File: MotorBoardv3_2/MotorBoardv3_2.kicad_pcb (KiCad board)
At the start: 2 copper layers, 128.3 x 158.1 mm, 98 parts, among them J1 Bump0, J11 GP2Y0A41SK0F, J12 GP2Y0A41SK0F, J13 GP2Y0A41SK0F, J15 7.2, J16 LP5.0, J17 ELA, J18 ERA, J19 Voltage Display, J2 Bump1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

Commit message: Filled in ground plane where needed
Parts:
- moved H10 174.5 mm to (58.9, 58.3)
- moved J20 45.6 mm to (68.6, 159.4), turned to 180 degrees
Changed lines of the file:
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@@
 		)
 		(pad "4" thru_hole oval
-			(at 0 -6.260001 280)
+			(at 0 -6.260002 280)
 			(size 4.699 1.778)
 			(drill oval 4.191 1.016)
@@
 	(footprint "RSLK2:54-00127_TEN"
 		(layer "F.Cu")
-		(at 98.689999 193.739955)
+		(at 68.600001 159.430045 180)
 		(tags "54-00127 ")
 		(property "Reference" "J20"
-			(at 4.650001 0 0)
+			(at 4.650001 0 180)
 			(unlocked yes)
 			(layer "F.SilkS")
@@
 		)
 		(property "Value" "Barrel_Jack"
-			(at 4.650001 0 0)
+			(at 4.650001 0 180)
 			(unlocked yes)
 			(layer "F.Fab")
@@
 		)
 		(property "Footprint" "RSLK2:54-00127_TEN"
-			(at 0 0 0)
+			(at 0 0 360)
 			(layer "F.Fab")
 			(hide yes)
@@
 		)
 		(property "Datasheet" ""
-			(at 0 0 0)
+			(at 0 0 360)
 			(layer "F.Fab")
 			(hide yes)
@@
 		)
 		(property "Description" "DC Barrel Jack"
-			(at 0 0 0)
+			(at 0 0 360)
 			(layer "F.Fab")
 			(hide yes)
@@
 		(attr smd)
 		(fp_line
-			(start -0.526999 -10.426954)
-			(end -0.526999 -9.016105)
+			(start 9.827001 1.333246)
+			(end 9.827001 -5.583806)
 			(stroke
 				(width 0.1524)
@@
 		)
 		(fp_line
-			(start -0.526999 -5.583806)
-			(end -0.526999 -1.438684)
+			(start 9.827001 -9.016105)
+			(end 9.827001 -10.426954)
 			(stroke
 				(width 0.1524)
@@
 		)
 		(fp_line
-			(start 0.666425 1.333246)
-			(end 2.733526 1.333246)
+			(start 9.827001 -10.426954)
+			(end -0.526999 -10.426954)
 			(stroke
 				(width 0.1524)
@@
 		)
 		(fp_line
-			(start 4.066476 1.333246)
-			(end 7.933576 1.333246)
+			(start 9.266425 1.333246)
+			(end 9.827001 1.333246)
 			(stroke
 				(width 0.1524)
@@
 		)
 		(fp_line
-			(start 4.523001 -10.426954)
-			(end 4.523001 -10.172954)
+			(start 4.777001 -10.172954)
+			(end 4.777001 -10.426954)
 			(stroke
 				(width 0.1524)
@@
 		)
 		(fp_line
-			(start 4.523001 -10.172954)
-			(end 4.777001 -10.172954)
+			(start 4.777001 -10.426954)
+			(end 4.523001 -10.426954)
 			(stroke
 				(width 0.1524)
@@
 		)
 		(fp_line
-			(start 4.777001 -10.426954)
-			(end 4.523001 -10.426954)
+			(start 4.523001 -10.172954)
+			(end 4.777001 -10.172954)
 			(stroke
 				(width 0.1524)
@@
 		)
 		(fp_line
-			(start 4.777001 -10.172954)
-			(end 4.777001 -10.426954)
+			(start 4.523001 -10.426954)
+			(end 4.523001 -10.172954)
 			(stroke
 				(width 0.1524)
@@
 		)
 		(fp_line
-			(start 9.266425 1.333246)
-			(end 9.827001 1.333246)
+			(start 4.066476 1.333246)
+			(end 7.933576 1.333246)
 			(stroke
 				(width 0.1524)
@@
 		)
 		(fp_line
-			(start 9.827001 -10.426954)
-			(end -0.526999 -10.426954)
+			(start 0.666425 1.333246)
+			(end 2.733526 1.333246)
 			(stroke
 				(width 0.1524)
@@
 		)
 		(fp_line
-			(start 9.827001 -9.016105)
-			(end 9.827001 -10.426954)
+			(start -0.526999 -5.583806)
+			(end -0.526999 -1.438684)
 			(stroke
 				(width 0.1524)
@@
 		)
 		(fp_line
-			(start 9.827001 1.333246)
-			(end 9.827001 -5.583806)
+			(start -0.526999 -10.426954)
+			(end -0.526999 -9.016105)
 			(stroke
 				(width 0.1524)
@@
 		)
 		(fp_line
-			(start -0.653999 -10.553954)
-			(end -0.653999 1.460246)
+			(start 9.954001 1.460246)
+			(end 9.954001 -10.553954)
 			(stroke
 				(width 0.1524)
@@
 		)
 		(fp_line
-			(start -0.653999 1.460246)
-			(end 9.954001 1.460246)
+			(start 9.954001 -10.553954)
+			(end -0.653999 -10.553954)
 			(stroke
 				(width 0.1524)
@@
 		)
 		(fp_line
-			(start 9.954001 -10.553954)
-			(end -0.653999 -10.553954)
+			(start -0.653999 1.460246)
+			(end 9.954001 1.460246)
 			(stroke
 				(width 0.1524)
@@
 		)
 		(fp_line
-			(start 9.954001 1.460246)
-			(end 9.954001 -10.553954)
+			(start -0.653999 -10.553954)
+			(end -0.653999 1.460246)
 			(stroke
 				(width 0.1524)
@@
 		)
 		(fp_line
-			(start -0.399999 -10.299954)
-			(end -0.399999 1.206246)
+			(start 9.700001 1.206246)
+			(end 9.700001 -10.299954)
 			(stroke
 				(width 0.0254)
@@
 		)
 		(fp_line
-			(start -0.399999 1.206246)
-			(end 9.700001 1.206246)
+			(start 9.700001 -10.299954)
+			(end -0.399999 -10.299954)
 			(stroke
 				(width 0.0254)
@@
 		)
 		(fp_line
-			(start 9.700001 -10.299954)
-			(end -0.399999 -10.299954)
+			(start -0.399999 1.206246)
+			(end 9.700001 1.206246)
 			(stroke
 				(width 0.0254)
@@
 		)
 		(fp_line
-			(start 9.700001 1.206246)
-			(end 9.700001 -10.299954)
+			(start -0.399999 -10.299954)
+			(end -0.399999 1.206246)
 			(stroke
 				(width 0.0254)
@@
 		)
 		(fp_text user "*"
-			(at -2.54 0 0)
+			(at -2.54 0 180)
 			(unlocked yes)
 			(layer "F.SilkS")
@@
 		)
 		(fp_text user "*"
-			(at -2.54 0 0)
+			(at -2.54 0 360)
 			(layer "F.SilkS")
 			(effects
@@
 		)
 		(fp_text user "*"
-			(at -2.54 0 0)
+			(at -2.54 0 360)
 			(layer "F.Fab")
 			(effects
@@
 		)
 		(fp_text user "${REFERENCE}"
-			(at 4.650001 0 0)
+			(at 4.650001 0 180)
 			(unlocked yes)
 			(layer "F.Fab")
@@
 		)
 		(fp_text user "*"
-			(at -2.54 0 0)
+			(at -2.54 0 180)
 			(unlocked yes)
 			(layer "F.Fab")
@@
 		)
 		(pad "" np_thru_hole circle
-			(at 3.300001 -6.299955)
+			(at 3.300001 -6.299955 180)
 			(size 2.54 2.54)
 			(drill 2.54)
@@
 		)
 		(pad "1" smd oval
-			(at 0 0)
+			(at 0 0 180)
 			(size 1.3208 2.5146)
 			(layers "F.Cu" "F.Paste" "F.Mask")
@@
 		)
 		(pad "2" smd oval
-			(at 8.600001 0)
+			(at 8.600001 0 180)
 			(size 1.3208 2.5146)
 			(layers "F.Cu" "F.Paste" "F.Mask")
@@
 		)
 		(pad "3" smd oval
-			(at 3.400001 0)
+			(at 3.400001 0 180)
 			(size 1.3208 2.5146)
 			(layers "F.Cu" "F.Paste" "F.Mask")
 		)
 		(pad "4" smd oval
-			(at -0.299999 -7.299955)
+			(at -0.299999 -7.299955 180)
 			(size 1.3208 2.8194)
 			(layers "F.Cu" "F.Paste" "F.Mask")
 		)
 		(pad "5" smd oval
-			(at 9.600001 -7.299955)
+			(at 9.600001 -7.299955 180)
 			(size 1.3208 2.8194)
 			(layers "F.Cu" "F.Paste" "F.Mask")
@@
 	(footprint "RSLK2:MountingHole_4_40"
 		(layer "F.Cu")
-		(at 231.71 82.86)
+		(at 58.92 58.31)
 		(descr "Mounting Hole 0.125in")
 		(tags "mounting hole 0.125in 4_40")
@@
 		(tags "mounting hole 0.125in 4_40")
 		(property "Reference" "H21"
-			(at 0 -4 0)
+			(at 0.05 11.2 0)
 			(layer "F.SilkS")
 			(effects
@@
 		)
 		(pad "4" thru_hole oval
-			(at 0 6.260001 260)
+			(at 0 6.260002 260)
 			(size 4.699 1.778)
 			(drill oval 4.191 1.016)
@@
 	)
 	(zone
+		(net 1)
+		(net_name "GND")
+		(layer "B.Cu")
+		(hatch edge 0.5)
+		(connect_pads
+			(clearance 0.5)
+		)
+		(min_thickness 0.25)
+		(filled_areas_thickness no)
+		(fill yes
+			(thermal_gap 0.5)
+			(thermal_bridge_width 0.5)
+		)
+		(polygon
+			(pts
+				(xy 50.16 156.83) (xy 58.45 170.2) (xy 107.31 182.26) (xy 159.52 167.26) (xy 166.71 156.87) (xy 162.56 156.85)
+				(xy 162.53 148.6) (xy 152.4 148.58) (xy 152.34 156.84) (xy 50.24 156.86)
+			)
+		)
+	)
+	(zone

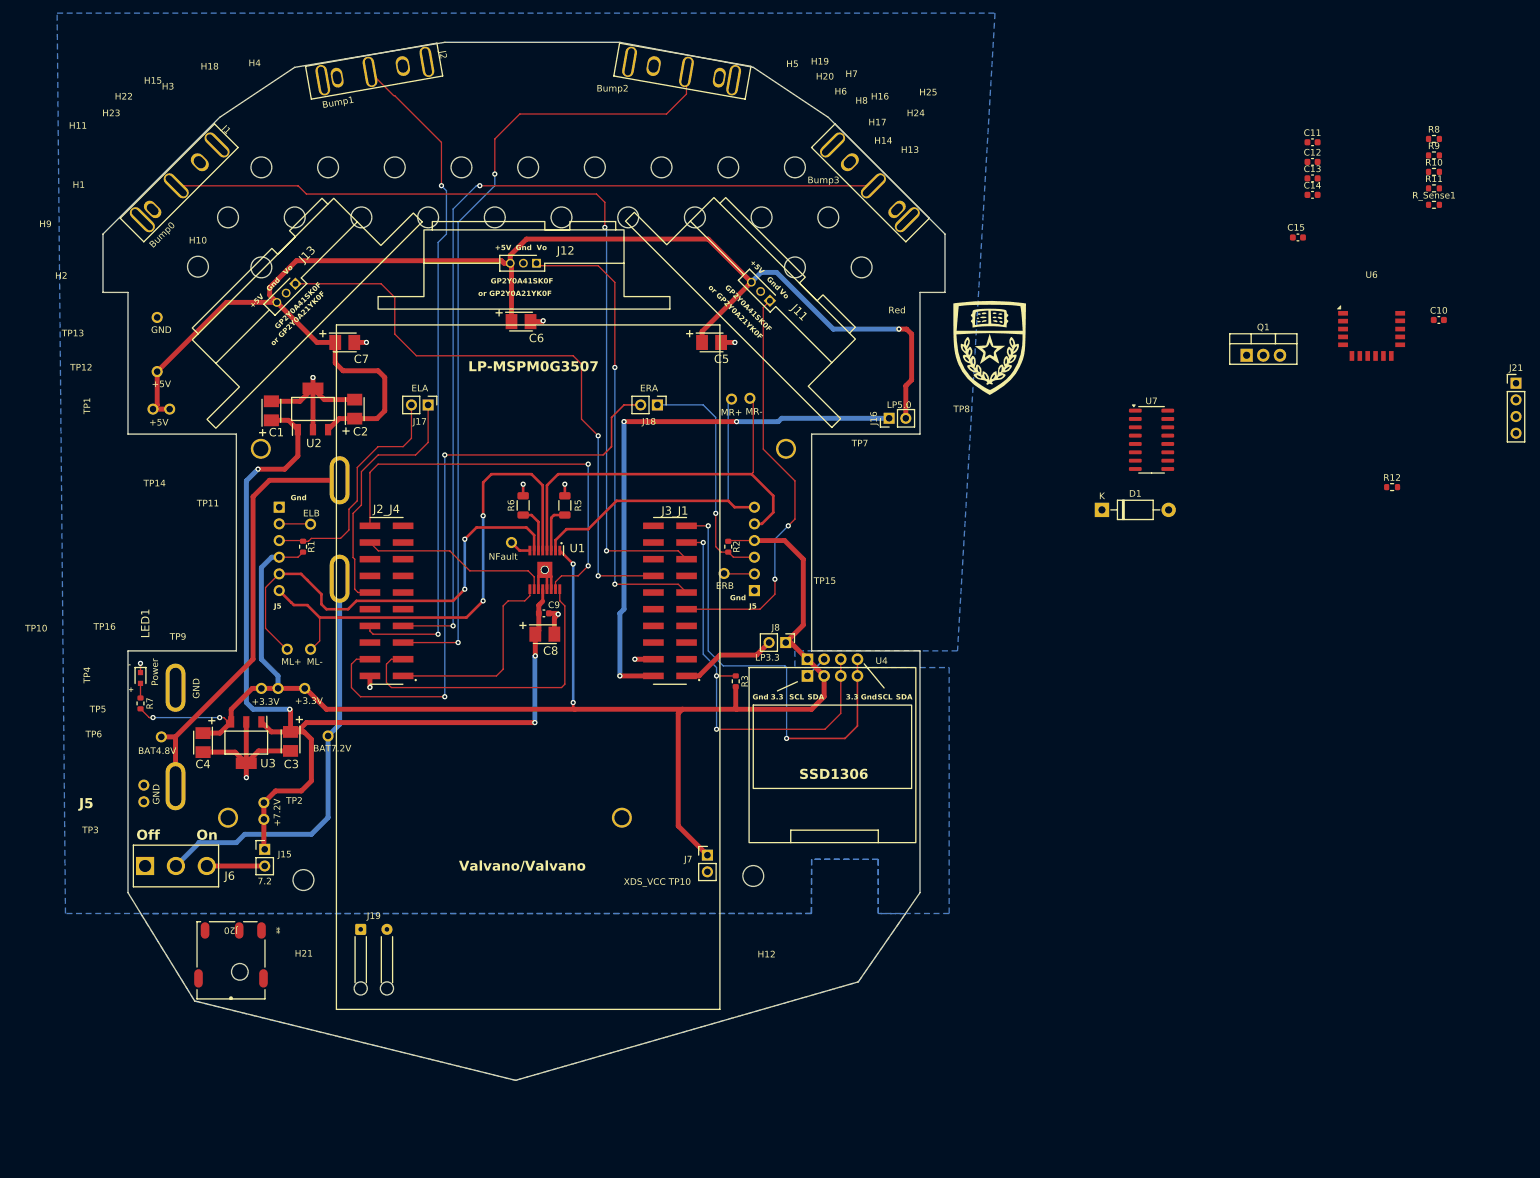
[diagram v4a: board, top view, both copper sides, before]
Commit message: Initial Charge Controller layout
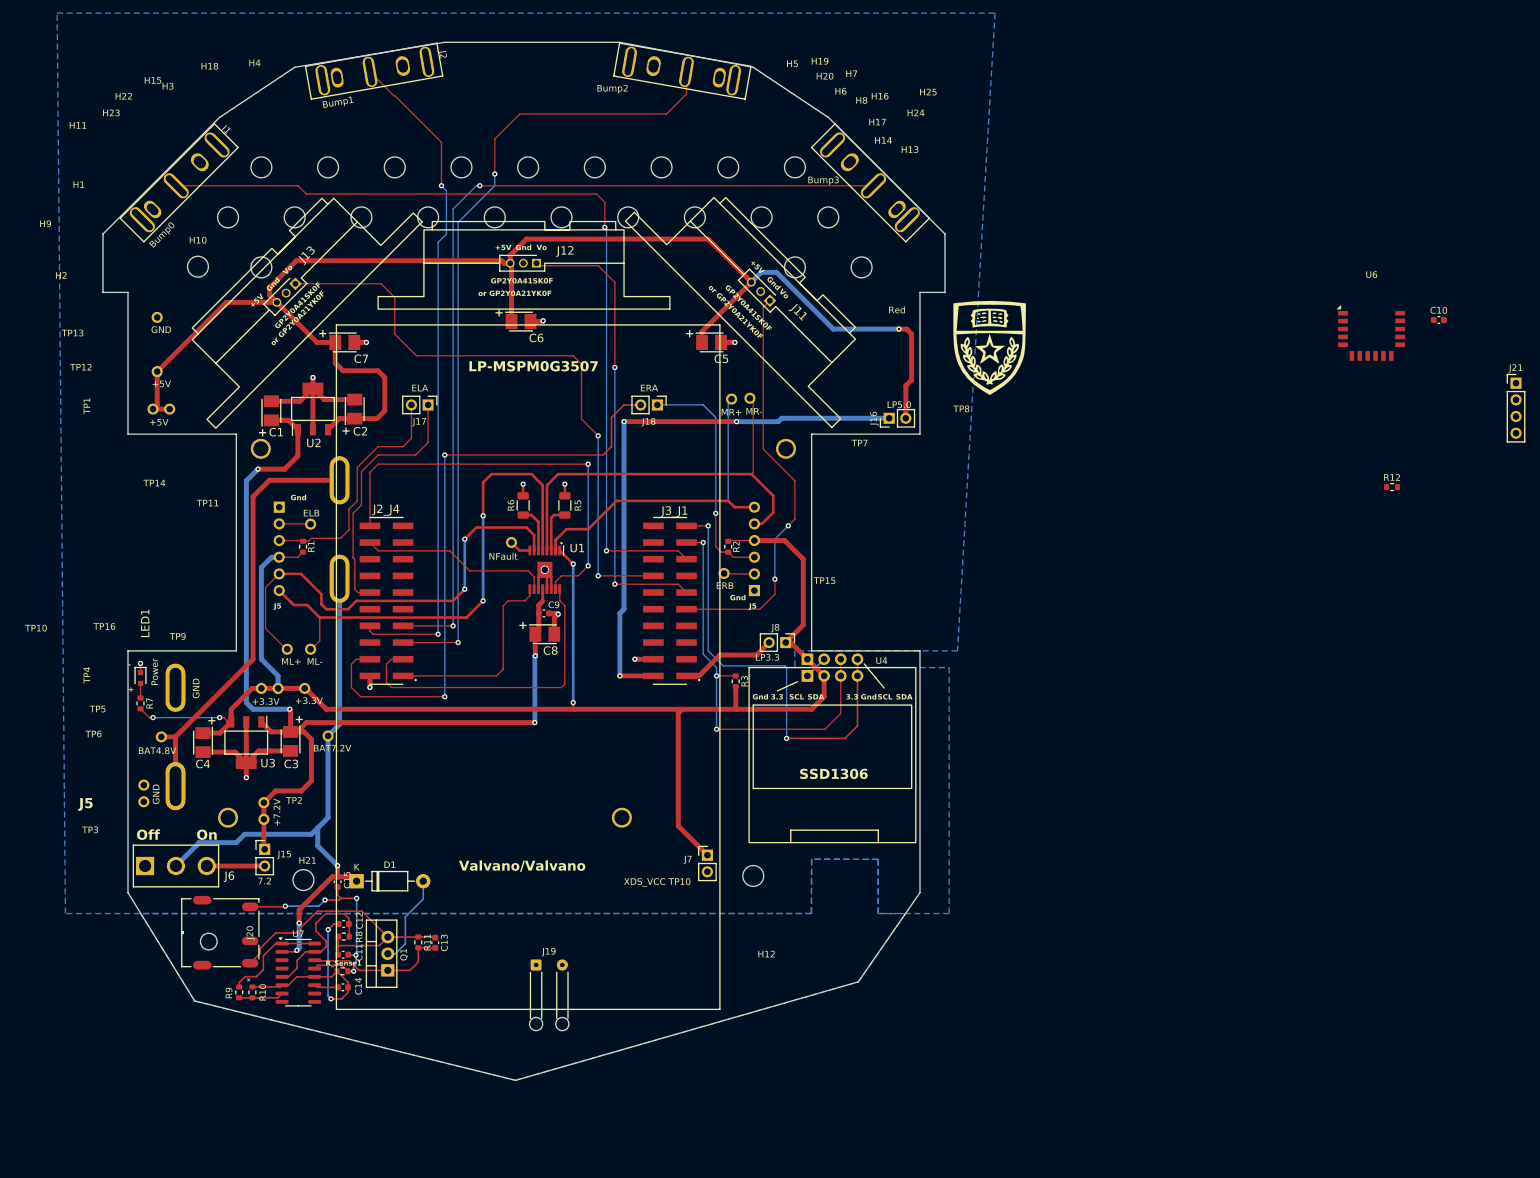
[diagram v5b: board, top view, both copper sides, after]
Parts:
- moved R9 222.2 mm to (65.2, 168.9), turned to -90 degrees
- moved R10 219.1 mm to (67.2, 168.9), turned to 90 degrees
- moved R8 205.8 mm to (81.1, 160.4)
- moved R_Sense1 203.2 mm to (80.9, 165.7)
- moved R11 192.7 mm to (92.5, 161.2), turned to -90 degrees
- moved C11 192.7 mm to (81.0, 163.1)
- moved C14 190.8 mm to (81.0, 168.1)
- moved C12 187.8 mm to (81.1, 158.4), turned to 180 degrees
- moved C13 177.3 mm to (95.1, 161.3), turned to -90 degrees
- moved C15 176.2 mm to (80.2, 152.0), turned to -90 degrees
- moved Q1 160.9 mm to (87.8, 165.5), turned to 90 degrees
- moved U7 153.2 mm to (74.2, 165.9)
- moved D1 126.9 mm to (83.1, 151.9)
- moved J19 27.3 mm to (110.4, 164.7)
- moved J20 5.28 mm to (66.9, 164.4), turned to 90 degrees
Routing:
- net Net-(Q1-E): track 0.00 -> 44.5 mm
- net Net-(U7-GND): track 0.00 -> 37.8 mm, vias 0 -> 5
- net GND: track 80.0 -> 113.5 mm, vias 12 -> 14
- net BAT7.2V: track 63.4 -> 91.9 mm, vias 0 -> 3
- net Net-(U7-THI): track 0.00 -> 22.6 mm
- net Net-(Q1-B): track 0.00 -> 21.7 mm
- net Net-(U7-REF): track 0.00 -> 15.9 mm
- net Net-(D1-A): track 0.00 -> 14.0 mm
- net Net-(U7-TEMP): track 0.00 -> 6.79 mm
- net Net-(U7-CC): track 0.00 -> 4.44 mm

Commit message: Label adjustements
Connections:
- net Net-(Q1-B) renamed /Charge Circuit/DRV
- net Net-(U7-REF) renamed /Charge Circuit/REF
- net Net-(U7-TEMP) renamed /Charge Circuit/TEMP
- net Net-(U7-THI) renamed /Charge Circuit/V+
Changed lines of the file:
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@@
 	(net 72 "Net-(Q1-E)")
 	(net 73 "Net-(U7-GND)")
-	(net 74 "Net-(U7-THI)")
-	(net 75 "Net-(Q1-B)")
+	(net 74 "/Charge Circuit/V+")
+	(net 75 "/Charge Circuit/DRV")
 	(net 76 "Net-(U7-CC)")
 	(net 77 "Net-(D1-A)")
-	(net 78 "Net-(U7-REF)")
-	(net 79 "Net-(U7-TEMP)")
+	(net 78 "/Charge Circuit/REF")
+	(net 79 "/Charge Circuit/TEMP")
 	(net 80 "unconnected-(U6-P1_7-Pad5)")
 	(net 81 "unconnected-(U6-RST-Pad10)")
@@
 			(layers "F.Cu" "F.Paste" "F.Mask")
 			(roundrect_rratio 0.25)
-			(net 74 "Net-(U7-THI)")
+			(net 74 "/Charge Circuit/V+")
 			(pintype "passive")
 		)
@@
 			(layers "F.Cu" "F.Paste" "F.Mask")
 			(roundrect_rratio 0.25)
-			(net 79 "Net-(U7-TEMP)")
+			(net 79 "/Charge Circuit/TEMP")
 			(pintype "passive")
 		)
@@
 			(layers "F.Cu" "F.Paste" "F.Mask")
 			(roundrect_rratio 0.25)
-			(net 75 "Net-(Q1-B)")
+			(net 75 "/Charge Circuit/DRV")
 			(pintype "passive")
 		)
@@
 			(layers "F.Cu" "F.Paste" "F.Mask")
 			(roundrect_rratio 0.25)
-			(net 74 "Net-(U7-THI)")
+			(net 74 "/Charge Circuit/V+")
 			(pintype "passive")
 		)
@@
 			(layers "*.Cu" "*.Mask")
 			(remove_unused_layers no)
-			(net 75 "Net-(Q1-B)")
+			(net 75 "/Charge Circuit/DRV")
 			(pinfunction "B")
 			(pintype "input")
@@
 			(layers "F.Cu" "F.Paste" "F.Mask")
 			(roundrect_rratio 0.25)
-			(net 78 "Net-(U7-REF)")
+			(net 78 "/Charge Circuit/REF")
 			(pinfunction "VLIMIT")
 			(pintype "input")
@@
 			(layers "F.Cu" "F.Paste" "F.Mask")
 			(roundrect_rratio 0.25)
-			(net 74 "Net-(U7-THI)")
+			(net 74 "/Charge Circuit/V+")
 			(pinfunction "THI")
 			(pintype "input")
@@
 			(layers "F.Cu" "F.Paste" "F.Mask")
 			(roundrect_rratio 0.25)
-			(net 79 "Net-(U7-TEMP)")
+			(net 79 "/Charge Circuit/TEMP")
 			(pinfunction "TEMP")
 			(pintype "input")
@@
 			(layers "F.Cu" "F.Paste" "F.Mask")
 			(roundrect_rratio 0.25)
-			(net 75 "Net-(Q1-B)")
+			(net 75 "/Charge Circuit/DRV")
 			(pinfunction "DRV")
 			(pintype "output")
@@
 			(layers "F.Cu" "F.Paste" "F.Mask")
 			(roundrect_rratio 0.25)
-			(net 74 "Net-(U7-THI)")
+			(net 74 "/Charge Circuit/V+")
 			(pinfunction "V+")
 			(pintype "power_in")
@@
 			(layers "F.Cu" "F.Paste" "F.Mask")
 			(roundrect_rratio 0.25)
-			(net 78 "Net-(U7-REF)")
+			(net 78 "/Charge Circuit/REF")
 			(pinfunction "REF")
 			(pintype "power_in")
@@
 			(layers "F.Cu" "F.Paste" "F.Mask")
 			(roundrect_rratio 0.25)
-			(net 75 "Net-(Q1-B)")
+			(net 75 "/Charge Circuit/DRV")
 			(pintype "passive")
 		)
@@
 			(layers "F.Cu" "F.Paste" "F.Mask")
 			(roundrect_rratio 0.25)
-			(net 78 "Net-(U7-REF)")
+			(net 78 "/Charge Circuit/REF")
 			(pintype "passive")
 		)
@@
 			(layers "F.Cu" "F.Paste" "F.Mask")
 			(roundrect_rratio 0.25)
-			(net 79 "Net-(U7-TEMP)")
+			(net 79 "/Charge Circuit/TEMP")
 			(pintype "passive")
 		)
